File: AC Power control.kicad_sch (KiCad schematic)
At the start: 24 parts, among them J10 USB_B_Micro, J9 Relay IO, U7 ULN2803CDWR, U8 USBLC6-2

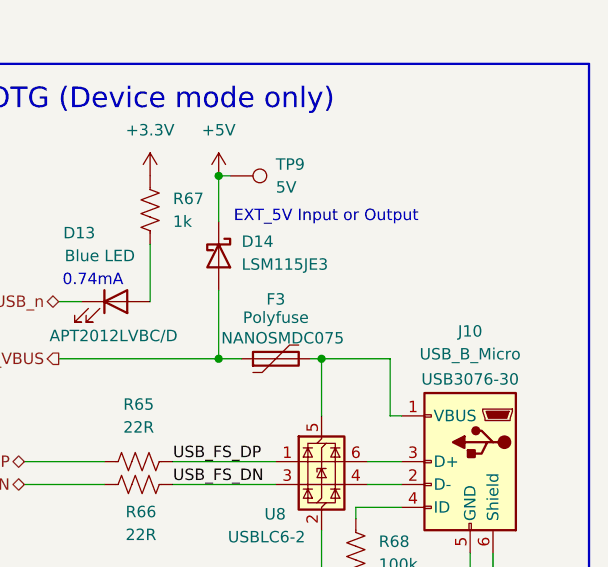
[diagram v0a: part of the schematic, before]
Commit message: Alternate MPNs added
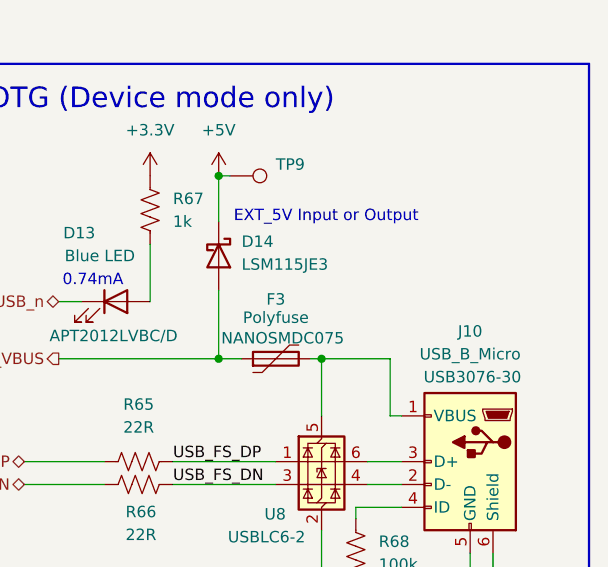
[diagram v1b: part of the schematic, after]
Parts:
- F3: MPN NANOSMDC075 -> NANOSMDC075F-2; Manufacturer_Part_Number (none) -> NANOSMDC075
- J10: MPN USB3076-30 -> USB3076-30-A; Manufacturer_Part_Number (none) -> USB3076-30
- TP9: value 5V -> TestPoint
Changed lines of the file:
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@@
 			)
 		)
-		(property "MPN" "NANOSMDC075"
+		(property "MPN" "NANOSMDC075F-2"
 			(at 235.712 84.074 90)
 			(effects
@@
 					(color 0 132 132 1)
 				)
+				(hide yes)
 			)
 		)
@@
 			)
 		)
-		(property "Manufacturer_Part_Number" ""
-			(at 234.95 86.36 90)
-			(effects
-				(font
-					(size 1.27 1.27)
-				)
-				(hide yes)
+		(property "Manufacturer_Part_Number" "NANOSMDC075"
+			(at 235.712 84.074 90)
+			(effects
+				(font
+					(size 1.27 1.27)
+					(color 0 132 132 1)
+				)
 			)
 		)
@@
 			)
 		)
-		(property "Value" "5V"
+		(property "Value" "TestPoint"
 			(at 234.95 67.3099 90)
 			(effects
@@
 				)
 				(justify left)
+				(hide yes)
 			)
 		)
@@
 			)
 		)
-		(property "MPN" "USB3076-30"
+		(property "MPN" "USB3076-30-A"
 			(at 256.54 88.646 0)
 			(effects
@@
 					(color 0 132 132 1)
 				)
-			)
-		)
-		(property "Manufacturer_Part_Number" ""
-			(at 256.54 97.79 0)
-			(effects
-				(font
-					(size 1.27 1.27)
-				)
-				(hide yes)
-			)
-		)
+				(hide yes)
+			)
+		)
+		(property "Manufacturer_Part_Number" "USB3076-30"
+			(at 256.794 88.392 0)
+			(effects
+				(font
+					(size 1.27 1.27)
+					(color 0 132 132 1)
+				)
+			)
+		)

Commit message: All comments addressed
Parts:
- added R69, R70: 0R, Resistor_SMD:R_0603_1608Metric, symbol Device:R_US
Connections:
- net +12V: now also R69.2; no longer J9.1 (Pin_1), U7.12 (COM)
- net +5V: now also R70.2; no longer D14.1 (K)
- new net: D14.1 (K), R70.1
- new net Earth: H1.1, H2.1, H3.1, H4.1
- new net V+: J9.1 (Pin_1), R69.1, U7.12 (COM)
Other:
- moved on the sheet: D14, F3
